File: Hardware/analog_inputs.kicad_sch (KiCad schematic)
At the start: 0 parts

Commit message: scheme update
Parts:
- added C31 (x2), C32, C33: 100n, Capacitor_SMD:C_0603_1608Metric_Pad1.08x0.95mm_HandSolder, symbol Device:C_Small
- added R40, R41: 100k, Resistor_SMD:R_0603_1608Metric_Pad0.98x0.95mm_HandSolder, symbol Device:R_Small
- added R44, R45: 1k, Resistor_SMD:R_0603_1608Metric_Pad0.98x0.95mm_HandSolder, symbol Device:R_Small
- added R48, R49, R50, R51: 20k, Resistor_SMD:R_0603_1608Metric_Pad0.98x0.95mm_HandSolder, symbol Device:R_Small
- added R56, R57, R60, R61: 10k, Resistor_SMD:R_0603_1608Metric_Pad0.98x0.95mm_HandSolder, symbol Device:R_Small
- added T11: TP_OP0_OUT, TestPoint:TestPoint_Pad_1.0x1.0mm, symbol Connector:TestPoint_Small
- added T12: TP_OP1_OUT, TestPoint:TestPoint_Pad_1.0x1.0mm, symbol Connector:TestPoint_Small
- added T15: TP_OP0_V-, TestPoint:TestPoint_Pad_1.0x1.0mm, symbol Connector:TestPoint_Small
- added T16: TP_OP1_V-, TestPoint:TestPoint_Pad_1.0x1.0mm, symbol Connector:TestPoint_Small
- added T19: TP_STEER_POS0, TestPoint:TestPoint_Pad_1.0x1.0mm, symbol Connector:TestPoint_Small
- added T20: TP_STEER_POS1, TestPoint:TestPoint_Pad_1.0x1.0mm, symbol Connector:TestPoint_Small
- added U11, U12: MCP6004, Package_SO:TSSOP-14_4.4x5mm_P0.65mm, symbol Amplifier_Operational:MCP6004
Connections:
- new net +5V: C31.1, C32.1, U11.4 (V+), U12.4 (V+)
- new net GND: C31.2, C31.2, C32.2, C33.2, R40.1, R41.1, R49.1, R51.1, R56.2, R57.2, U11.11 (V-), U12.11 (V-)
- new net IN_STEER_POS0: R40.2, R44.1
- new net IN_STEER_POS1: R41.2, R45.1
- new net OP0_IN: C33.1, R44.2, U11.3 (+)
- new net OP0_OUT: R48.1, T11.1, U11.1, U11.2 (-)
- new net OP0_V+: R48.2, R56.1, U12.3 (+)
- new net OP0_V-: R49.2, R60.2, T15.1, U12.2 (-)
- new net OP1_IN: C31.1, R45.2, U11.5 (+)
- new net OP1_OUT: R50.1, T12.1, U11.6 (-), U11.7
- new net OP1_V+: R50.2, R57.1, U12.5 (+)
- new net OP1_V-: R51.2, R61.2, T16.1, U12.6 (-)
- new net STEER_POS0: R60.1, T19.1, U12.1
- new net STEER_POS1: R61.1, T20.1, U12.7
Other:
- note added: "ANALOG SIGNALS"
- note added: "OP AMPS POWER"
- title: (none) -> PLC ON STM

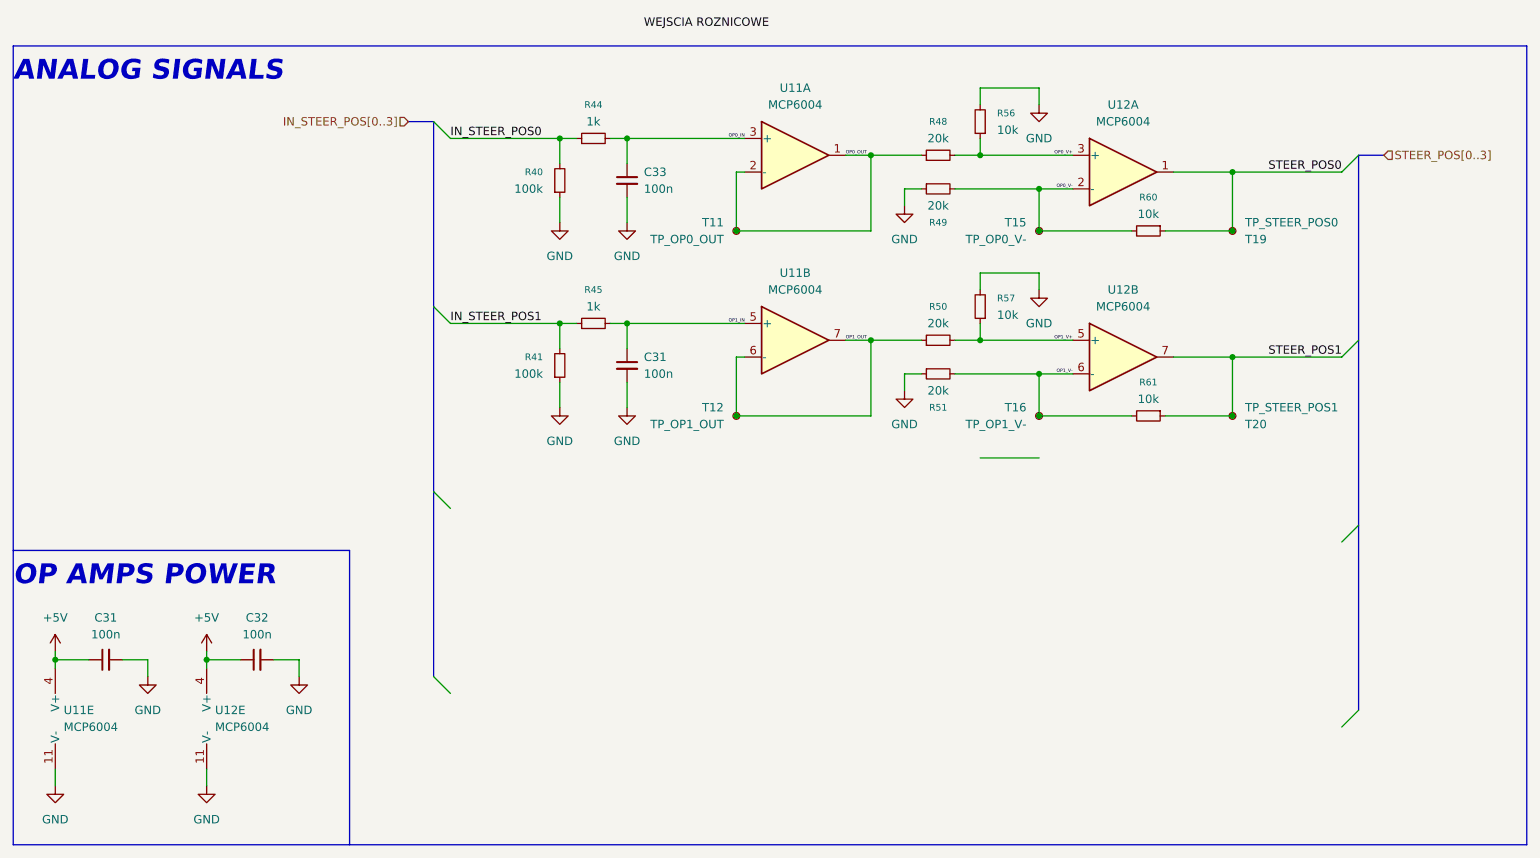
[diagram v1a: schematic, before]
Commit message: schematic update
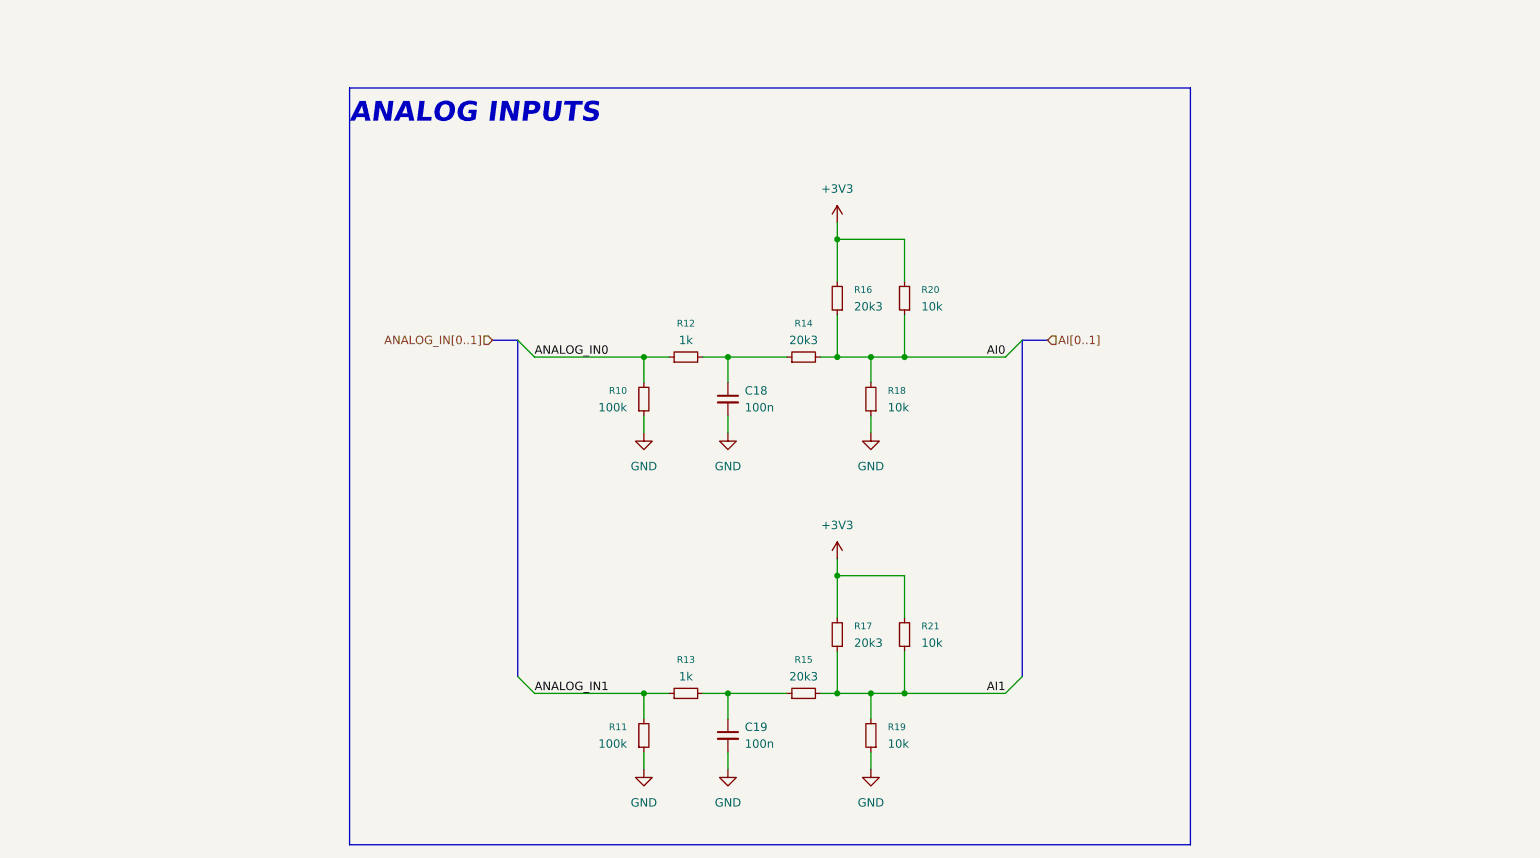
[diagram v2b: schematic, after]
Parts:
- removed C31 (x2), C32, C33: 100n, Capacitor_SMD:C_0603_1608Metric_Pad1.08x0.95mm_HandSolder, symbol Device:C_Small
- removed R40, R41: 100k, Resistor_SMD:R_0603_1608Metric_Pad0.98x0.95mm_HandSolder, symbol Device:R_Small
- removed R44, R45: 1k, Resistor_SMD:R_0603_1608Metric_Pad0.98x0.95mm_HandSolder, symbol Device:R_Small
- removed R48, R49, R50, R51: 20k, Resistor_SMD:R_0603_1608Metric_Pad0.98x0.95mm_HandSolder, symbol Device:R_Small
- removed R56, R57, R60, R61: 10k, Resistor_SMD:R_0603_1608Metric_Pad0.98x0.95mm_HandSolder, symbol Device:R_Small
- removed T11: TP_OP0_OUT, TestPoint:TestPoint_Pad_1.0x1.0mm, symbol Connector:TestPoint_Small
- removed T12: TP_OP1_OUT, TestPoint:TestPoint_Pad_1.0x1.0mm, symbol Connector:TestPoint_Small
- removed T15: TP_OP0_V-, TestPoint:TestPoint_Pad_1.0x1.0mm, symbol Connector:TestPoint_Small
- removed T16: TP_OP1_V-, TestPoint:TestPoint_Pad_1.0x1.0mm, symbol Connector:TestPoint_Small
- removed T19: TP_STEER_POS0, TestPoint:TestPoint_Pad_1.0x1.0mm, symbol Connector:TestPoint_Small
- removed T20: TP_STEER_POS1, TestPoint:TestPoint_Pad_1.0x1.0mm, symbol Connector:TestPoint_Small
- removed U11, U12: MCP6004, Package_SO:TSSOP-14_4.4x5mm_P0.65mm, symbol Amplifier_Operational:MCP6004
- added C18, C19: 100n, Capacitor_SMD:C_0603_1608Metric_Pad1.08x0.95mm_HandSolder, symbol Device:C_Small
- added R10, R11: 100k, Resistor_SMD:R_0603_1608Metric_Pad0.98x0.95mm_HandSolder, symbol Device:R_Small
- added R12, R13: 1k, Resistor_SMD:R_0603_1608Metric_Pad0.98x0.95mm_HandSolder, symbol Device:R_Small
- added R14, R15, R16, R17: 20k3, Resistor_SMD:R_0603_1608Metric_Pad0.98x0.95mm_HandSolder, symbol Device:R_Small
- added R18, R19, R20, R21: 10k, Resistor_SMD:R_0603_1608Metric_Pad0.98x0.95mm_HandSolder, symbol Device:R_Small
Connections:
- net GND: now also C18.2, C19.2, R10.1, R11.1, R18.1, R19.1
- new net: C19.1, R13.2, R15.1
- new net: C18.1, R12.2, R14.1
- new net +3V3: R16.2, R17.2, R20.2, R21.2
- new net AI0: R14.2, R16.1, R18.2, R20.1
- new net AI1: R15.2, R17.1, R19.2, R21.1
- new net ANALOG_IN0: R10.2, R12.1
- new net ANALOG_IN1: R11.2, R13.1
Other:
- note added: "ANALOG INPUTS"
- note removed: "ANALOG SIGNALS"
- note removed: "OP AMPS POWER"
